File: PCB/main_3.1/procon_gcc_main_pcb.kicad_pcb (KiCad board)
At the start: 4 copper layers, 110.9 x 59.7 mm, 136 parts, among them J1 Conn_01x04_Pin, J2 SM02B-SURS-TF_LF__SN_, J3 To Button Board, J4 SM02B-SURS-TF_LF__SN_, J5 Conn_01x02_Pin, J9 USB_C_Receptacle, Q4 BSS138DW, Q5 BSS138DW, Q7 MMBT3904, Q8 MMBT3904, SW1 GL18_SW, SW2 GL18_SW, SW3 1TS026A-1000-0550, SW4 TS35CA, SW5 1TS026A-1000-0550, T1 36-8730, T2 36-8730, T3 36-8730, T4 36-8730, U1 GH39F (Hall SOT23), U10 MCP3002, U11 ST_LSM6, U12 PI3USB4000A, U13 GD25Q80EEIGR, U14 TPS630001RCR, U15 DRV2605LYZFR, U16 BQ25180, U2 GH39F (Hall SOT23), U3 GH39F (Hall SOT23), U4 GH39F (Hall SOT23), U5 ST_LSM6, U6 RP2040, U7 CH340K, U8 MCP3002, U9 ESP32-PICO-MINI-02, Y1 Crystal_GND3

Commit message: Update 4.7.2023
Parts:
- moved C28 1.49 mm to (90.6, 136.4)
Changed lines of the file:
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@@
   (net 143 "Net-(L12-DOUT)")
   (footprint "Capacitor_SMD:C_0201_0603Metric" (layer "F.Cu")
-    (at 89.6 135.375 180)
+    (at 90.6272 136.4488 180)
     (descr "Capacitor SMD 0201 (0603 Metric), square (rectangular) end terminal, IPC_7351 nominal, (Body size source: https://www.vishay.com/docs/20052/crcw0201e3.pdf), generated with kicad-footprint-generator")
     (tags "capacitor")
@@
   (segment (start 154.91 106.75) (end 154.91 107.8184) (width 0.4) (layer "B.Cu") (net 15))
   (segment (start 152.305746 110.7694) (end 151.6888 110.7694) (width 0.2) (layer "F.Cu") (net 16))
-  (segment (start 89.2744 138.721493) (end 89.2744 134.7536) (width 0.4) (layer "F.Cu") (net 16))
+  (segment (start 90.3072 137.688693) (end 90.3072 133.7208) (width 0.4) (layer "F.Cu") (net 16))
+  (segment (start 89.2744 138.721493) (end 90.3072 137.688693) (width 0.4) (layer "F.Cu") (net 16))
   (segment (start 86.125 137.275) (end 87.827907 137.275) (width 0.25) (layer "F.Cu") (net 16))
   (segment (start 84.6328 134.6708) (end 84.6328 135.7828) (width 0.25) (layer "F.Cu") (net 16))
@@
   (segment (start 87.827907 137.275) (end 89.2744 138.721493) (width 0.25) (layer "F.Cu") (net 16))
   (segment (start 83.9338 133.9718) (end 84.6328 134.6708) (width 0.25) (layer "F.Cu") (net 16))
+  (segment (start 90.3072 133.7208) (end 90.424 133.604) (width 0.4) (layer "F.Cu") (net 16))
   (segment (start 89.2744 140.1826) (end 89.2744 138.721493) (width 0.4) (layer "F.Cu") (net 16))
-  (segment (start 89.2744 134.7536) (end 90.424 133.604) (width 0.4) (layer "F.Cu") (net 16))
   (segment (start 83.0072 133.9718) (end 83.9338 133.9718) (width 0.25) (layer "F.Cu") (net 16))
   (segment (start 152.618203 111.081857) (end 152.305746 110.7694) (width 0.2) (layer "F.Cu") (net 16))

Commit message: PCB and FW Updates
- Add player number support internally
- Add debug for bt baseband updating
- Orange indication for baseband update mode
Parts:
- turned C16 to 0 degrees
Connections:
- C16 pad 1: GND -> Net-(D2-A)
- C16 pad 2: Net-(D2-A) -> GND

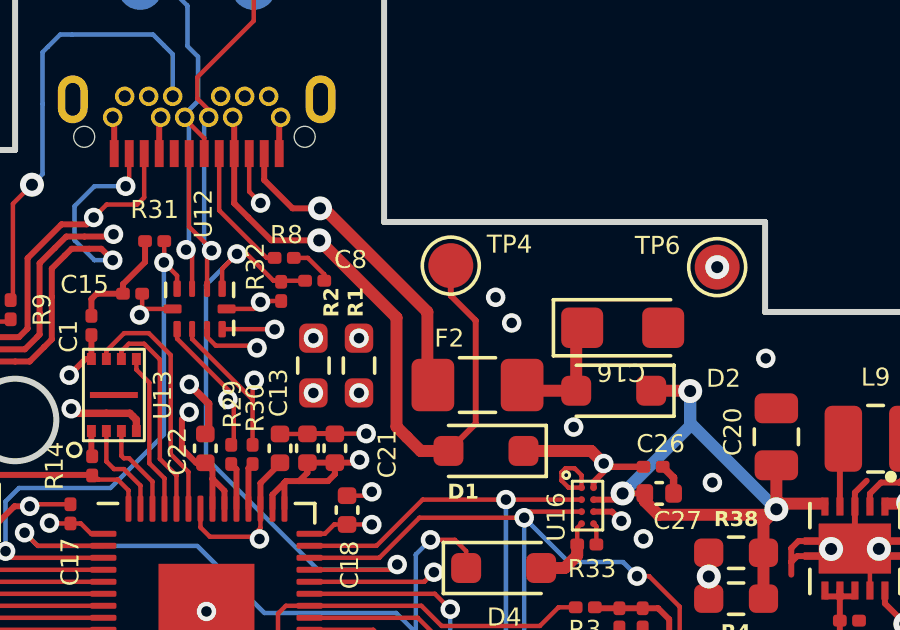
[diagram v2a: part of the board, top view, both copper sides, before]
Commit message: 5.16.2024 update
N64 Fixes
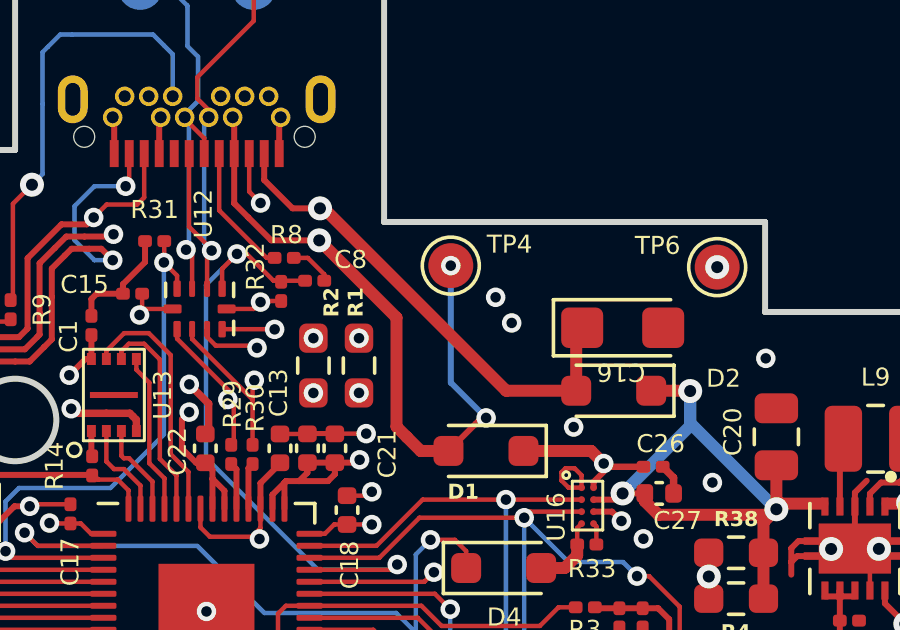
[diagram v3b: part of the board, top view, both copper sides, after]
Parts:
- removed F2: Fuse, Fuse:Fuse_1206_3216Metric_Pad1.42x1.75mm_HandSolder
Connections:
- C16 pad 1: Net-(D2-A) -> +3.3V_PRE
- D2 pad 2: Net-(D2-A) -> +3.3V_PRE
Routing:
- net +3.3V_PRE: track 26.6 -> 32.3 mm
- net Net-(D2-A): track 4.06 -> 0.00 mm
- net VBUS_PRE: track 27.4 -> 27.8 mm, vias 1 -> 3

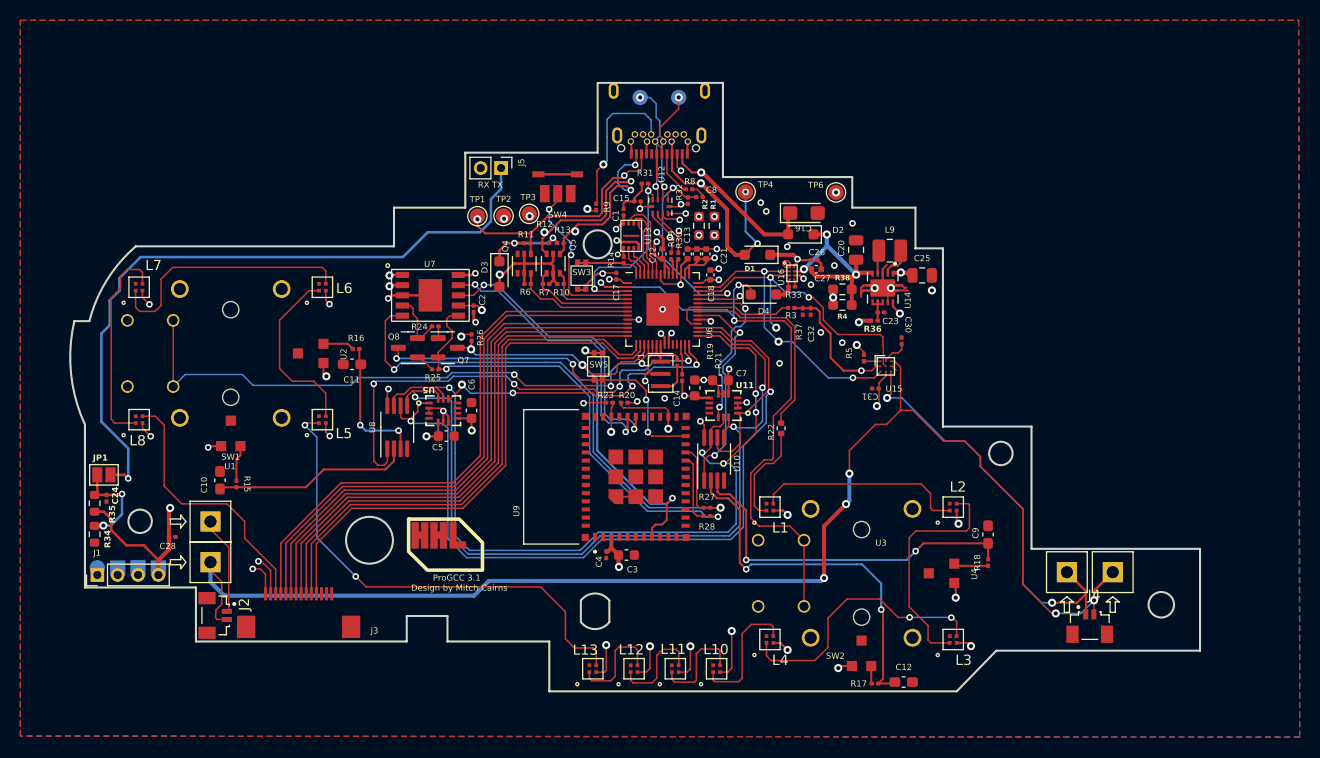
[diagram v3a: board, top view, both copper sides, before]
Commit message: Fix PCB Main
- Move main ribbon connector left to avoid collision issue
- Move ribbon connector to support new ribbon placement
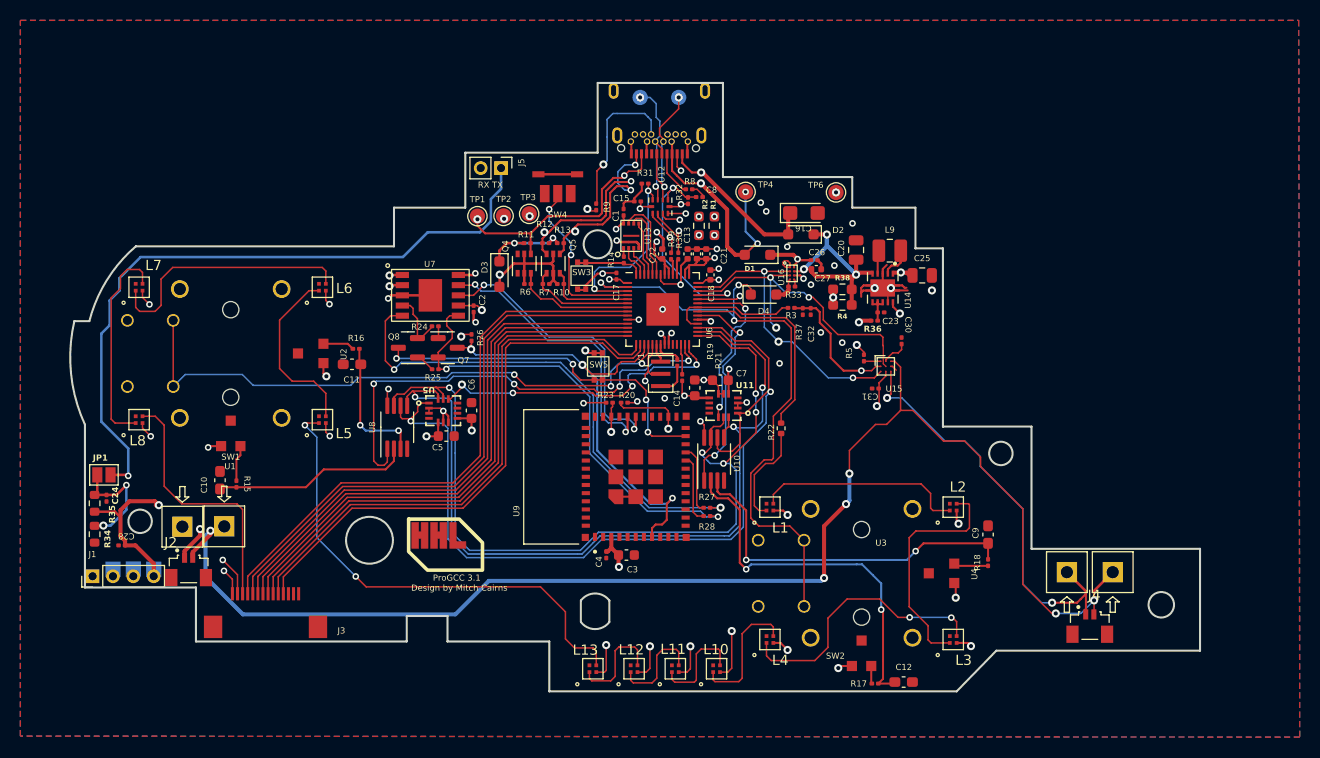
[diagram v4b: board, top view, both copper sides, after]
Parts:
- removed the REF** at (83.3, 139.5)
- moved J2 6.80 mm to (92.2, 138.5), turned to 0 degrees
- moved C28 5.02 mm to (85.7, 137.3), turned to 0 degrees
- moved T2 3.77 mm to (95.7, 135.4), turned to 180 degrees
- moved J3 3.25 mm to (99.8, 145.3)
- moved T3 2.80 mm to (91.6, 135.4), turned to 180 degrees
- moved ? 0.48 mm to (88.8, 139.6)
- moved ? 0.48 mm to (86.8, 139.6)
- moved REF** 0.48 mm to (84.8, 139.6)
- moved J1 0.48 mm to (82.8, 140.3)
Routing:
- net LRA_OUT_+: track 134.1 -> 136.6 mm, vias 5 -> 6
- net LRA_OUT_-: track 136.2 -> 134.2 mm, vias 2 -> 3
- net BAT_LVL: track 85.8 -> 87.6 mm
- net Scan_D: track 53.1 -> 54.4 mm
- net Scan_C: track 54.6 -> 55.9 mm
- net Scan_B: track 52.4 -> 53.7 mm
- net Push_D: track 53.2 -> 54.6 mm
- net Push_C: track 51.7 -> 53.1 mm
- net Push_B: track 53.7 -> 55.1 mm
- net Push_A: track 55.3 -> 56.6 mm
- net Scan_A: track 53.2 -> 54.5 mm
- net BATTERY_POS: track 91.8 -> 92.7 mm
- net GND: track 71.6 -> 70.8 mm
- net BUTTON_RGB: track 26.2 -> 25.4 mm

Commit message: update r2 label
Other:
- board text added: "ProGCC 3.1 r2"
- board text removed: "ProGCC 3.1"
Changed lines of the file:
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@@
 		)
 	)
-	(gr_text "ProGCC 3.1"
-		(at 118.57 140.462 0)
+	(gr_text "ProGCC 3.1 r2"
+		(at 118.34 140.49 0)
 		(layer "F.SilkS")
 		(effects

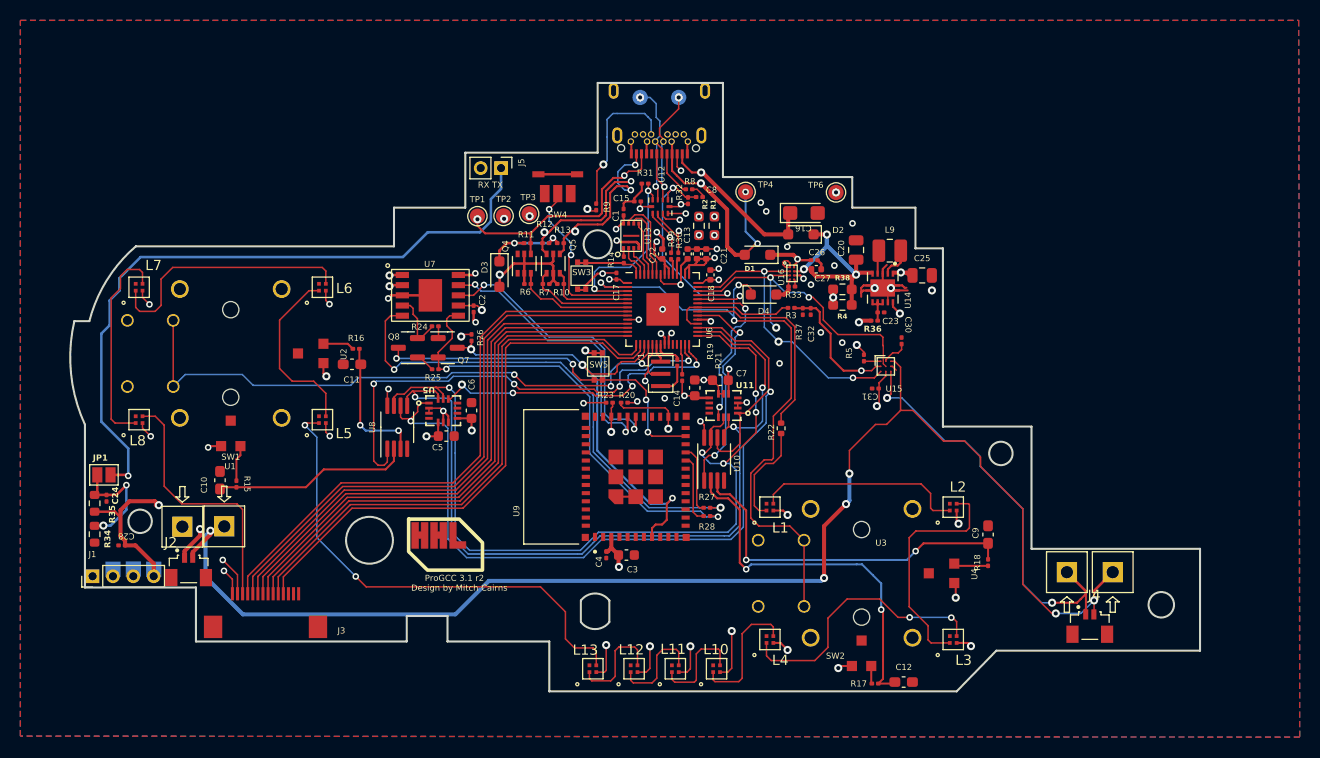
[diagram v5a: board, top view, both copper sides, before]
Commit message: PCB revision
- Exchange G18 sticks for newer iteration with TMR sensing
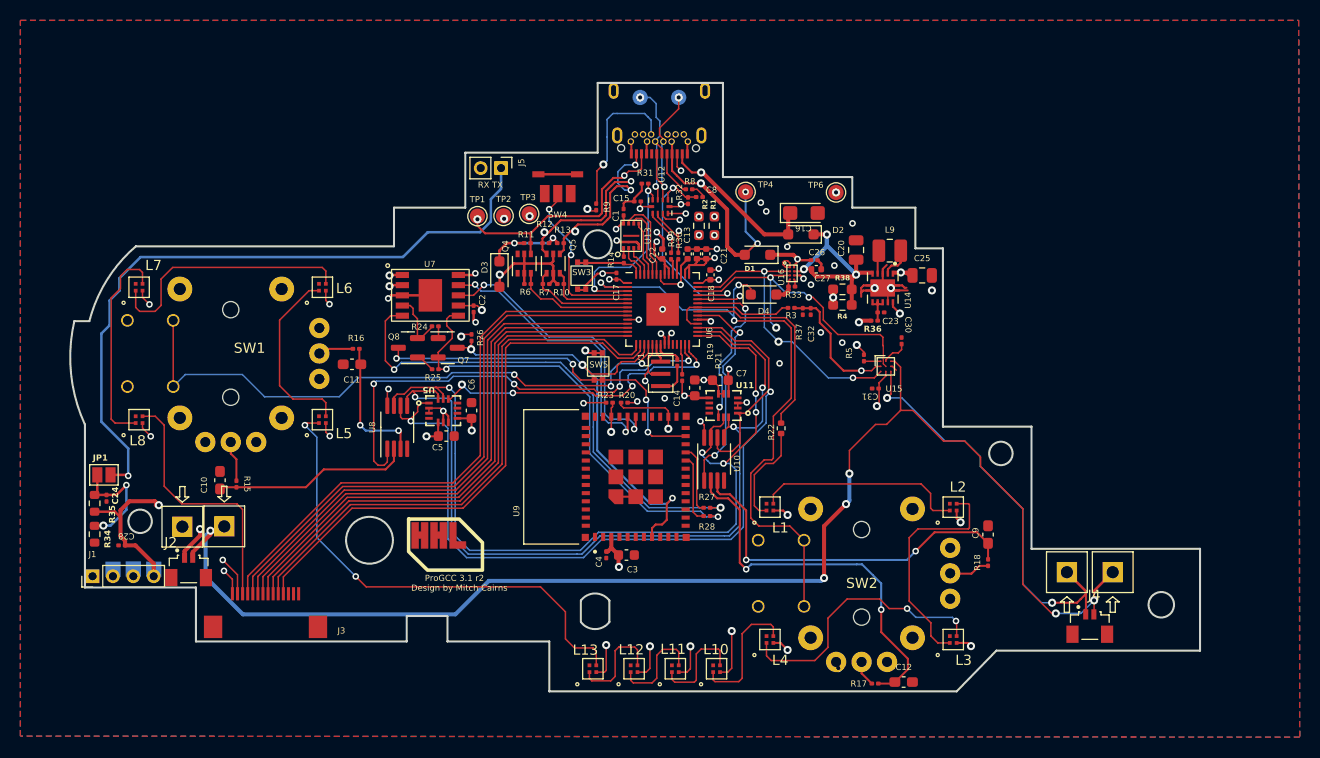
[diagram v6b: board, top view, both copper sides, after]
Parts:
- removed U1, U2, U3, U4: GH39F (Hall SOT23), hhl:GH39F
- SW1, SW2: value GL18_SW -> GL1807SYAE-002; footprint hhl:GL18 -> hhl:GL1807SYAE
- U14: value TPS630001RCR -> TPS63001DRCR
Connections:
- R15 pad 1: Net-(U1-VOUT) -> Net-(SW1-X_OUT)
- R16 pad 1: Net-(U2-VOUT) -> Net-(SW1-Y_OUT)
- R17 pad 1: Net-(U3-VOUT) -> Net-(SW2-X_OUT)
- R18 pad 1: Net-(U4-VOUT) -> Net-(SW2-Y_OUT)
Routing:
- net +3V3: track 110.9 -> 105.2 mm, vias 44 -> 40
- net Net-(SW2-Y_OUT): track 0.00 -> 4.05 mm
- net Net-(SW1-X_OUT): track 0.00 -> 4.03 mm
- net Net-(U1-VOUT): track 3.56 -> 0.00 mm
- net Net-(SW1-Y_OUT): track 0.00 -> 3.48 mm
- net Net-(U4-VOUT): track 3.41 -> 0.00 mm
- net Net-(U2-VOUT): track 3.09 -> 0.00 mm
- net Net-(SW2-X_OUT): track 0.00 -> 2.54 mm
- net Net-(U3-VOUT): track 1.75 -> 0.00 mm
- net RX: track 36.8 -> 38.3 mm
- net LS_BUTTON: track 58.4 -> 59.4 mm
- net RY: track 35.5 -> 36.4 mm
- net GND: track 70.8 -> 71.7 mm, vias 29 -> 30
